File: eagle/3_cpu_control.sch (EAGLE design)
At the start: 50 parts, among them IC1 74LS151N, IC10 74LS173N, IC11 74LS74N, IC12 74LS74N, IC13 74LS541N, IC14 74LS541N, IC15 74LS21N, IC16 74LS02N, IC17 74LS02N, IC18 74LS04N, IC2 74LS151N, IC20 74LS08N, IC3 74LS153N, IC4 74LS153N, IC5 74LS541N, IC6 74LS32N, IC7 74LS08N, IC8 74LS151N, IC9 74LS157N

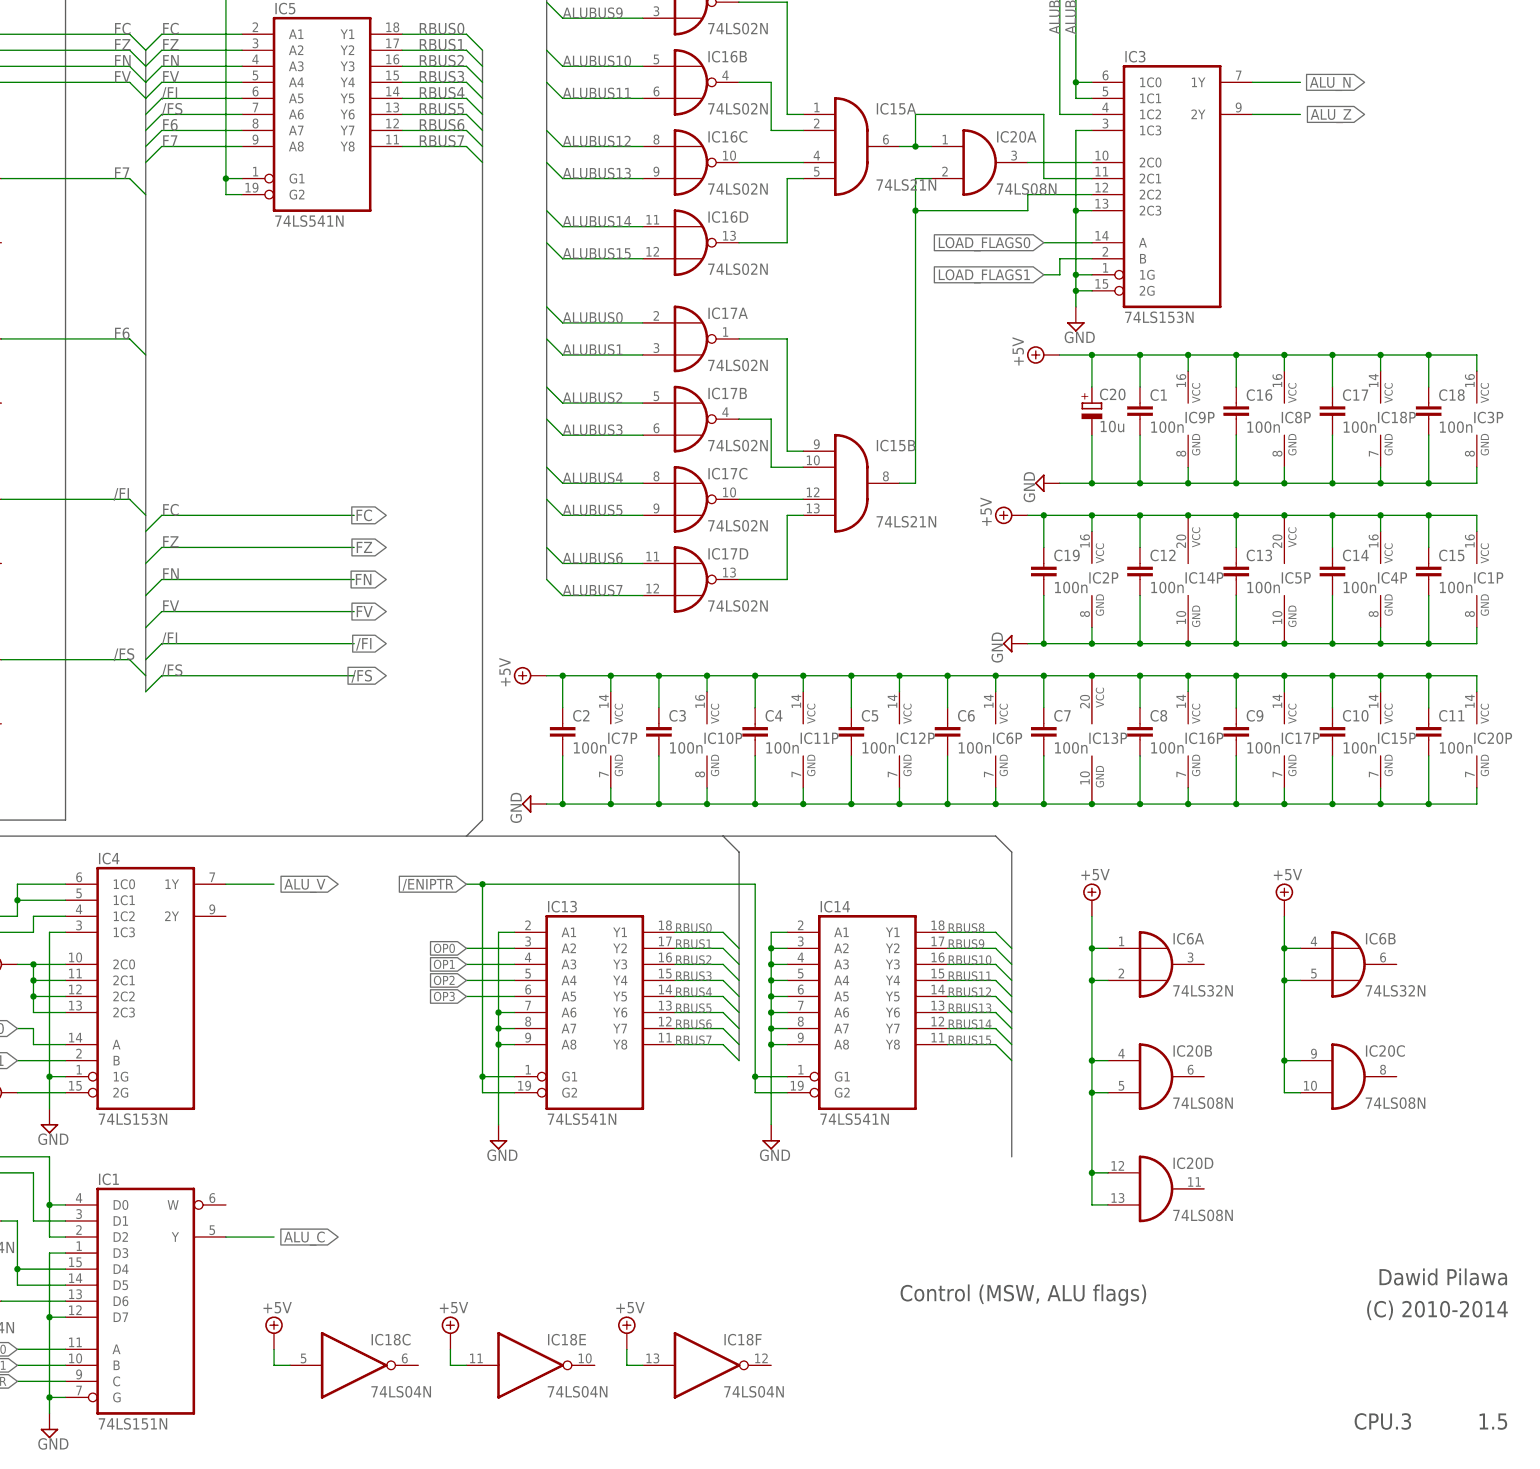
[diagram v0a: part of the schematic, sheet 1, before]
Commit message: Renamed F6 to /FP
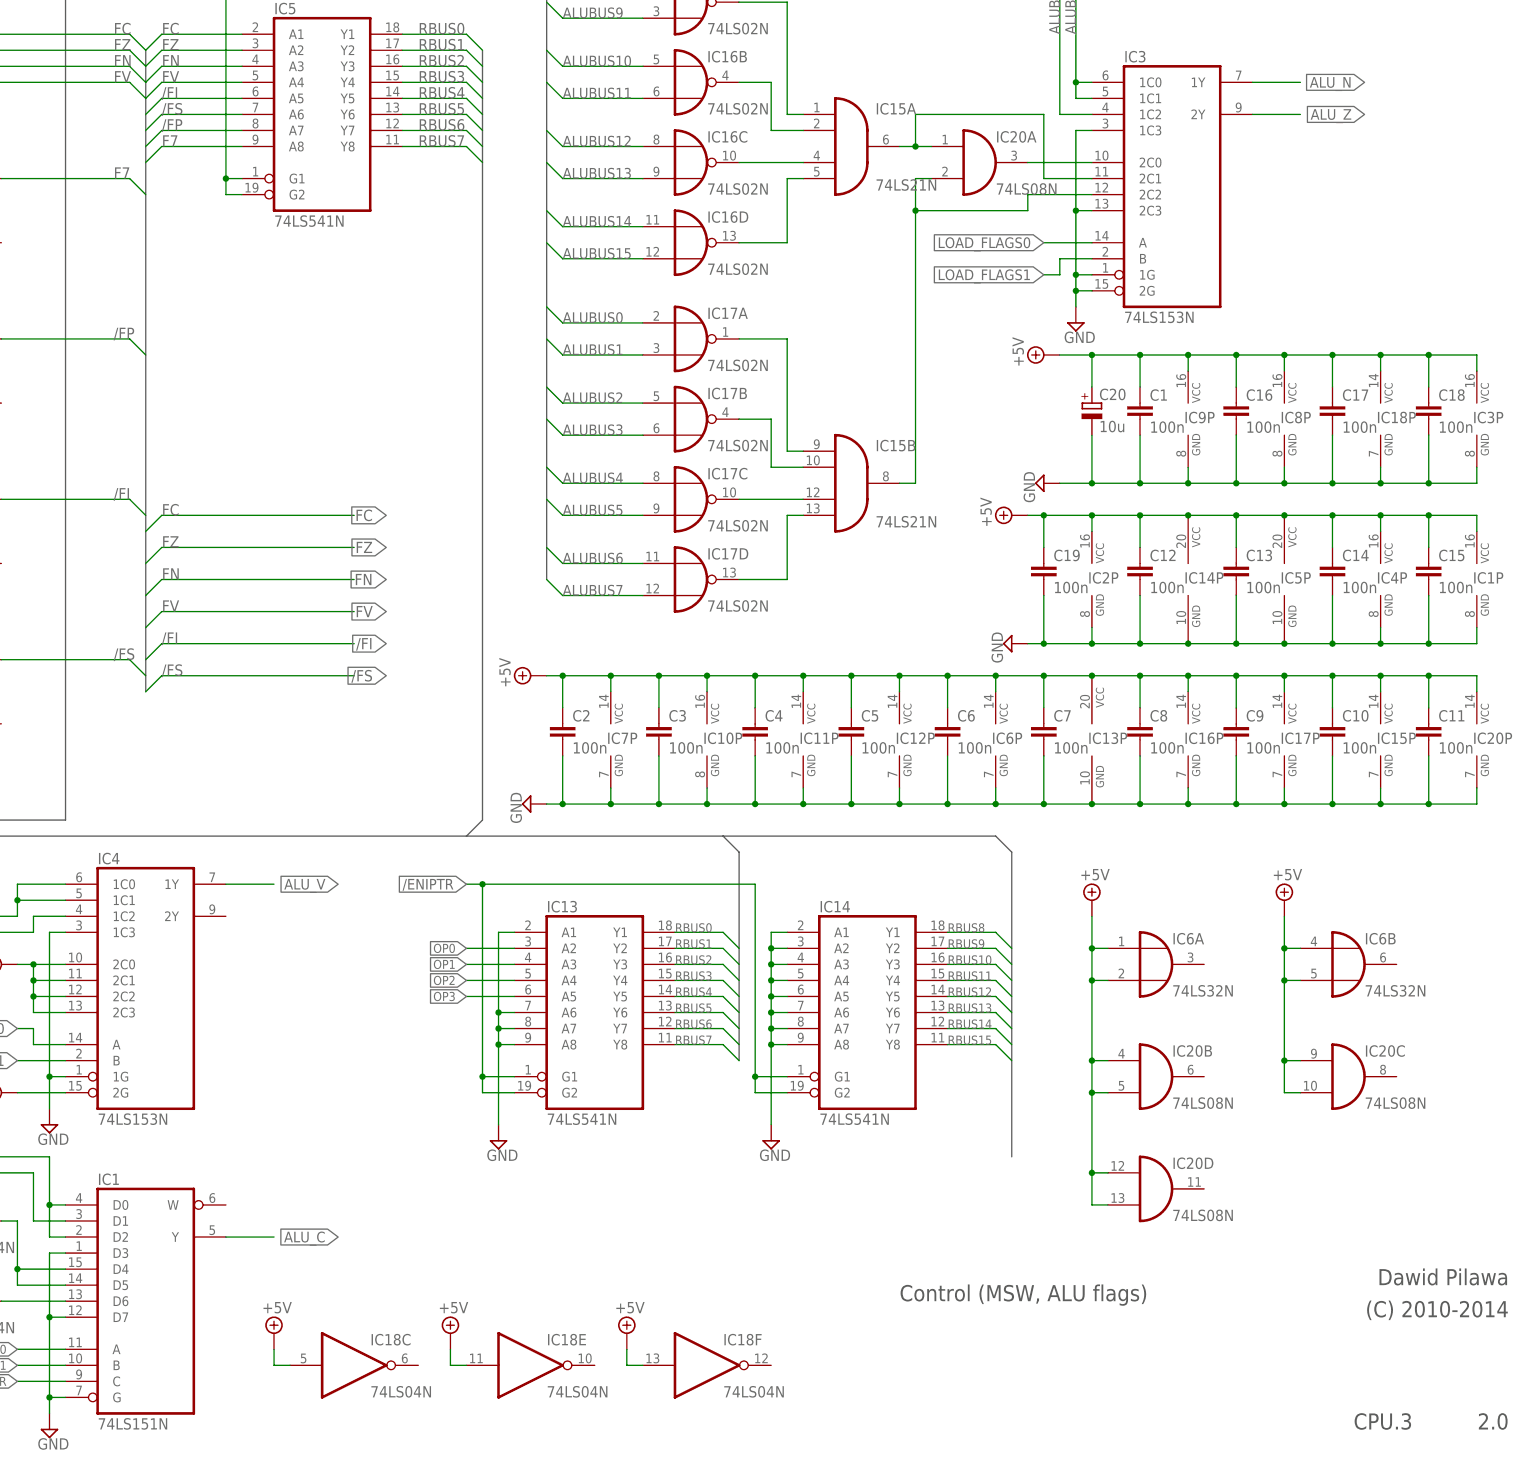
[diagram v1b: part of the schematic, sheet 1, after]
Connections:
- net F6 renamed /FP
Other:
- note added: "2.0"
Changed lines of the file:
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@@
 <plain>
 <text x="111.76" y="-111.76" size="2.54" layer="97" font="vector">Control (MSW, ALU flags)</text>
-<text x="208.28" y="-129.54" size="2.54" layer="97" font="vector" rot="R180">1.5</text>
+<text x="208.28" y="-129.54" size="2.54" layer="97" font="vector" rot="R180">2.0</text>
 <text x="208.28" y="-106.68" size="2.54" layer="97" font="vector" rot="R180">Dawid Pilawa</text>
 <text x="208.28" y="-111.76" size="2.54" layer="97" font="vector" rot="R180">(C) 2010-2014</text>
@@
 </segment>
 </net>
-<net name="F6" class="0">
+<net name="/FP" class="0">
 <segment>
 <wire x1="-7.62" y1="71.12" x2="-5.08" y2="73.66" width="0.1524" layer="91"/>

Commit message: Added /FP (flag paging enabled) to schematics and board, extended header connector
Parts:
- JP10: device pinhead:PINHD-2X16 -> pinhead:PINHD-2X18
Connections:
- net +5V: no longer IC11B.PRE
- net /FP: now also JP10.34
- net /RST: now also IC11B.PRE
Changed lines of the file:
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@@
 <part name="JP3" library="pinhead" deviceset="PINHD-2X8" device=""/>
 <part name="JP4" library="pinhead" deviceset="PINHD-2X8" device=""/>
-<part name="JP10" library="pinhead" deviceset="PINHD-2X16" device=""/>
+<part name="JP10" library="pinhead" deviceset="PINHD-2X18" device=""/>
 <part name="JP9" library="pinhead" deviceset="PINHD-2X24" device=""/>
 <part name="JP7" library="pinhead" deviceset="PINHD-1X9" device=""/>
@@
 </segment>
 </bus>
-<bus name="FC,FZ,FN,FV,/FI,/FS,F6,F7">
+<bus name="FC,FZ,FN,FV,/FI,/FS,/FP,F7">
 <segment>
-<wire x1="-7.62" y1="86.36" x2="-7.62" y2="-15.24" width="0.762" layer="92"/>
+<wire x1="-7.62" y1="86.36" x2="-7.62" y2="-17.78" width="0.762" layer="92"/>
 </segment>
 </bus>
@@
 <wire x1="-147.32" y1="33.02" x2="-147.32" y2="7.62" width="0.1524" layer="91"/>
 <wire x1="-147.32" y1="7.62" x2="-142.24" y2="7.62" width="0.1524" layer="91"/>
-<wire x1="-147.32" y1="33.02" x2="-66.04" y2="33.02" width="0.1524" layer="91"/>
-<wire x1="-66.04" y1="33.02" x2="-55.88" y2="33.02" width="0.1524" layer="91"/>
-<wire x1="-66.04" y1="33.02" x2="-66.04" y2="58.42" width="0.1524" layer="91"/>
-<wire x1="-66.04" y1="58.42" x2="-55.88" y2="58.42" width="0.1524" layer="91"/>
+<wire x1="-147.32" y1="33.02" x2="-71.12" y2="33.02" width="0.1524" layer="91"/>
+<wire x1="-71.12" y1="33.02" x2="-55.88" y2="33.02" width="0.1524" layer="91"/>
+<wire x1="-71.12" y1="33.02" x2="-71.12" y2="58.42" width="0.1524" layer="91"/>
+<wire x1="-71.12" y1="58.42" x2="-55.88" y2="58.42" width="0.1524" layer="91"/>
 <wire x1="-142.24" y1="-17.78" x2="-147.32" y2="-17.78" width="0.1524" layer="91"/>
 <wire x1="-147.32" y1="-17.78" x2="-147.32" y2="7.62" width="0.1524" layer="91"/>
 <junction x="-147.32" y="66.04"/>
 <junction x="-147.32" y="38.1"/>
-<junction x="-66.04" y="33.02"/>
+<junction x="-71.12" y="33.02"/>
 <junction x="-147.32" y="33.02"/>
 <junction x="-147.32" y="7.62"/>
@@
 <pinref part="IC12" gate="B" pin="CLR"/>
 <pinref part="IC12" gate="A" pin="PRE"/>
+<wire x1="-66.04" y1="15.24" x2="-66.04" y2="40.64" width="0.1524" layer="91"/>
+<pinref part="IC11" gate="B" pin="PRE"/>
+<wire x1="-66.04" y1="40.64" x2="-55.88" y2="40.64" width="0.1524" layer="91"/>
 </segment>
 </net>
@@
 </segment>
 <segment>
-<wire x1="-7.62" y1="10.16" x2="-5.08" y2="12.7" width="0.1524" layer="91"/>
-<wire x1="-5.08" y1="12.7" x2="25.4" y2="12.7" width="0.1524" layer="91"/>
-<label x="30.48" y="12.7" size="1.778" layer="95" rot="R180" xref="yes"/>
-<label x="-5.08" y="12.7" size="1.778" layer="95"/>
+<wire x1="-7.62" y1="12.7" x2="-5.08" y2="15.24" width="0.1524" layer="91"/>
+<wire x1="-5.08" y1="15.24" x2="25.4" y2="15.24" width="0.1524" layer="91"/>
+<label x="30.48" y="15.24" size="1.778" layer="95" rot="R180" xref="yes"/>
+<label x="-5.08" y="15.24" size="1.778" layer="95"/>
 </segment>
 <segment>
@@
 </segment>
 <segment>
-<wire x1="-7.62" y1="5.08" x2="-5.08" y2="7.62" width="0.1524" layer="91"/>
-<wire x1="-5.08" y1="7.62" x2="25.4" y2="7.62" width="0.1524" layer="91"/>
-<label x="30.48" y="7.62" size="1.778" layer="95" rot="R180" xref="yes"/>
-<label x="-5.08" y="7.62" size="1.778" layer="95"/>
+<wire x1="-7.62" y1="7.62" x2="-5.08" y2="10.16" width="0.1524" layer="91"/>
+<wire x1="-5.08" y1="10.16" x2="25.4" y2="10.16" width="0.1524" layer="91"/>
+<label x="30.48" y="10.16" size="1.778" layer="95" rot="R180" xref="yes"/>
+<label x="-5.08" y="10.16" size="1.778" layer="95"/>
 </segment>
 <segment>
@@
 </segment>
 <segment>
-<wire x1="-7.62" y1="0" x2="-5.08" y2="2.54" width="0.1524" layer="91"/>
-<wire x1="-5.08" y1="2.54" x2="25.4" y2="2.54" width="0.1524" layer="91"/>
-<label x="30.48" y="2.54" size="1.778" layer="95" rot="R180" xref="yes"/>
-<label x="-5.08" y="2.54" size="1.778" layer="95"/>
+<wire x1="-7.62" y1="2.54" x2="-5.08" y2="5.08" width="0.1524" layer="91"/>
+<wire x1="-5.08" y1="5.08" x2="25.4" y2="5.08" width="0.1524" layer="91"/>
+<label x="30.48" y="5.08" size="1.778" layer="95" rot="R180" xref="yes"/>
+<label x="-5.08" y="5.08" size="1.778" layer="95"/>
 </segment>
 <segment>
@@
 </segment>
 <segment>
-<wire x1="-7.62" y1="-5.08" x2="-5.08" y2="-2.54" width="0.1524" layer="91"/>
-<wire x1="-5.08" y1="-2.54" x2="25.4" y2="-2.54" width="0.1524" layer="91"/>
-<label x="30.48" y="-2.54" size="1.778" layer="95" rot="R180" xref="yes"/>
-<label x="-5.08" y="-2.54" size="1.778" layer="95"/>
+<wire x1="-7.62" y1="-2.54" x2="-5.08" y2="0" width="0.1524" layer="91"/>
+<wire x1="-5.08" y1="0" x2="25.4" y2="0" width="0.1524" layer="91"/>
+<label x="30.48" y="0" size="1.778" layer="95" rot="R180" xref="yes"/>
+<label x="-5.08" y="0" size="1.778" layer="95"/>
 </segment>
 <segment>
@@
 </segment>
 <segment>
-<wire x1="-7.62" y1="-10.16" x2="-5.08" y2="-7.62" width="0.1524" layer="91"/>
-<wire x1="-5.08" y1="-7.62" x2="25.4" y2="-7.62" width="0.1524" layer="91"/>
-<label x="30.48" y="-7.62" size="1.778" layer="95" rot="R180" xref="yes"/>
-<label x="-5.08" y="-7.62" size="1.778" layer="95"/>
+<wire x1="-7.62" y1="-7.62" x2="-5.08" y2="-5.08" width="0.1524" layer="91"/>
+<wire x1="-5.08" y1="-5.08" x2="25.4" y2="-5.08" width="0.1524" layer="91"/>
+<label x="30.48" y="-5.08" size="1.778" layer="95" rot="R180" xref="yes"/>
+<label x="-5.08" y="-5.08" size="1.778" layer="95"/>
 </segment>
 <segment>
@@
 <pinref part="IC11" gate="B" pin="Q"/>
 </segment>
+<segment>
+<wire x1="-7.62" y1="-17.78" x2="-5.08" y2="-15.24" width="0.1524" layer="91"/>
+<wire x1="-5.08" y1="-15.24" x2="25.4" y2="-15.24" width="0.1524" layer="91"/>
+<label x="30.48" y="-15.24" size="1.778" layer="95" rot="R180" xref="yes"/>
+</segment>
 </net>
 <net name="F7" class="0">
@@
 </segment>
 <segment>
-<wire x1="-7.62" y1="-15.24" x2="-5.08" y2="-12.7" width="0.1524" layer="91"/>
-<wire x1="-5.08" y1="-12.7" x2="25.4" y2="-12.7" width="0.1524" layer="91"/>
-<label x="30.48" y="-12.7" size="1.778" layer="95" rot="R180" xref="yes"/>
-<label x="-5.08" y="-12.7" size="1.778" layer="95"/>
+<wire x1="-7.62" y1="-12.7" x2="-5.08" y2="-10.16" width="0.1524" layer="91"/>
+<wire x1="-5.08" y1="-10.16" x2="25.4" y2="-10.16" width="0.1524" layer="91"/>
+<label x="30.48" y="-10.16" size="1.778" layer="95" rot="R180" xref="yes"/>
+<label x="-5.08" y="-10.16" size="1.778" layer="95"/>
 </segment>
 <segment>
@@
 </segment>
 <segment>
-<wire x1="-58.42" y1="40.64" x2="-55.88" y2="40.64" width="0.1524" layer="91"/>
-<wire x1="-58.42" y1="30.48" x2="-58.42" y2="40.64" width="0.1524" layer="91"/>
+<wire x1="-58.42" y1="30.48" x2="-58.42" y2="43.18" width="0.1524" layer="91"/>
 <wire x1="-58.42" y1="30.48" x2="-55.88" y2="30.48" width="0.1524" layer="91"/>
-<wire x1="-58.42" y1="40.64" x2="-58.42" y2="43.18" width="0.1524" layer="91"/>
-<junction x="-58.42" y="40.64"/>
-<pinref part="IC11" gate="B" pin="PRE"/>
 <pinref part="IC11" gate="B" pin="CLR"/>
 <pinref part="SUPPLY29" gate="+5V" pin="+5V"/>
@@
 <instance part="JP3" gate="A" x="154.94" y="226.06"/>
 <instance part="JP4" gate="A" x="154.94" y="187.96"/>
-<instance part="JP10" gate="A" x="86.36" y="134.62"/>
+<instance part="JP10" gate="A" x="86.36" y="132.08"/>
 <instance part="JP9" gate="A" x="86.36" y="68.58"/>
 <instance part="JP7" gate="A" x="167.64" y="142.24"/>
@@
 </segment>
 </net>
+<net name="/FP" class="0">
+<segment>
+<pinref part="JP10" gate="A" pin="34"/>
+<wire x1="91.44" y1="111.76" x2="101.6" y2="111.76" width="0.1524" layer="91"/>
+<label x="101.6" y="111.76" size="1.27" layer="95" xref="yes"/>
+</segment>
+</net>

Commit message: All boards prepared for MMU extension
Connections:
- new net /IO: JP10.35
- new net /NP_FAULT: JP10.36
- new net /WR_FAULT: JP10.33
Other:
- note removed: "1.5"
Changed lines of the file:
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@@
 <plain>
 <text x="289.56" y="27.94" size="2.54" layer="97" font="vector">Control (MSW, ALU flags)</text>
-<text x="386.08" y="10.16" size="2.54" layer="97" font="vector" rot="R180">1.5</text>
+<text x="386.08" y="10.16" size="2.54" layer="97" font="vector" rot="R180">2.0</text>
 <text x="386.08" y="33.02" size="2.54" layer="97" font="vector" rot="R180">Dawid Pilawa</text>
 <text x="386.08" y="27.94" size="2.54" layer="97" font="vector" rot="R180">(C) 2010-2014</text>
@@
 </segment>
 </net>
+<net name="/WR_FAULT" class="0">
+<segment>
+<pinref part="JP10" gate="A" pin="33"/>
+<wire x1="83.82" y1="111.76" x2="73.66" y2="111.76" width="0.1524" layer="91"/>
+<label x="73.66" y="111.76" size="1.27" layer="95" rot="R180" xref="yes"/>
+</segment>
+</net>
+<net name="/NP_FAULT" class="0">
+<segment>
+<pinref part="JP10" gate="A" pin="36"/>
+<wire x1="91.44" y1="109.22" x2="101.6" y2="109.22" width="0.1524" layer="91"/>
+<label x="101.6" y="109.22" size="1.27" layer="95" xref="yes"/>
+</segment>
+</net>
+<net name="/IO" class="0">
+<segment>
+<pinref part="JP10" gate="A" pin="35"/>
+<wire x1="83.82" y1="109.22" x2="73.66" y2="109.22" width="0.1524" layer="91"/>
+<label x="73.66" y="109.22" size="1.27" layer="95" rot="R180" xref="yes"/>
+</segment>
+</net>

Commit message: MMU schematics update
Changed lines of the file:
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@@
 <wire x1="-5.08" y1="-15.24" x2="25.4" y2="-15.24" width="0.1524" layer="91"/>
 <label x="30.48" y="-15.24" size="1.778" layer="95" rot="R180" xref="yes"/>
+<label x="-5.08" y="-15.24" size="1.778" layer="95"/>
 </segment>
 </net>

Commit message: Removal of PPC started
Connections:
- removed net /LDPPC: JP10.11
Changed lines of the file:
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@@
-</segment>
-</net>
-<net name="/LDPPC" class="0">
-<segment>
-<pinref part="JP10" gate="A" pin="11"/>
-<wire x1="83.82" y1="139.7" x2="73.66" y2="139.7" width="0.1524" layer="91"/>
-<label x="73.66" y="139.7" size="1.27" layer="95" rot="R180" xref="yes"/>
 </segment>
 </net>
